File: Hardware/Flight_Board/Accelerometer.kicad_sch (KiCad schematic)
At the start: 6 parts, among them U3 ADXL375

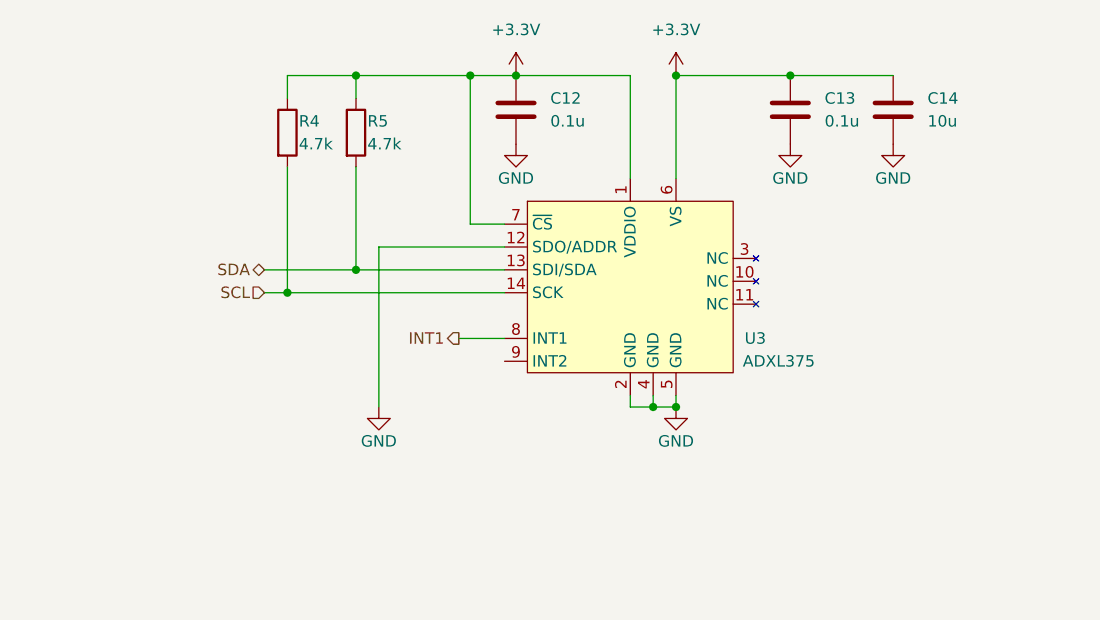
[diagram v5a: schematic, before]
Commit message: Add LEDs and test points
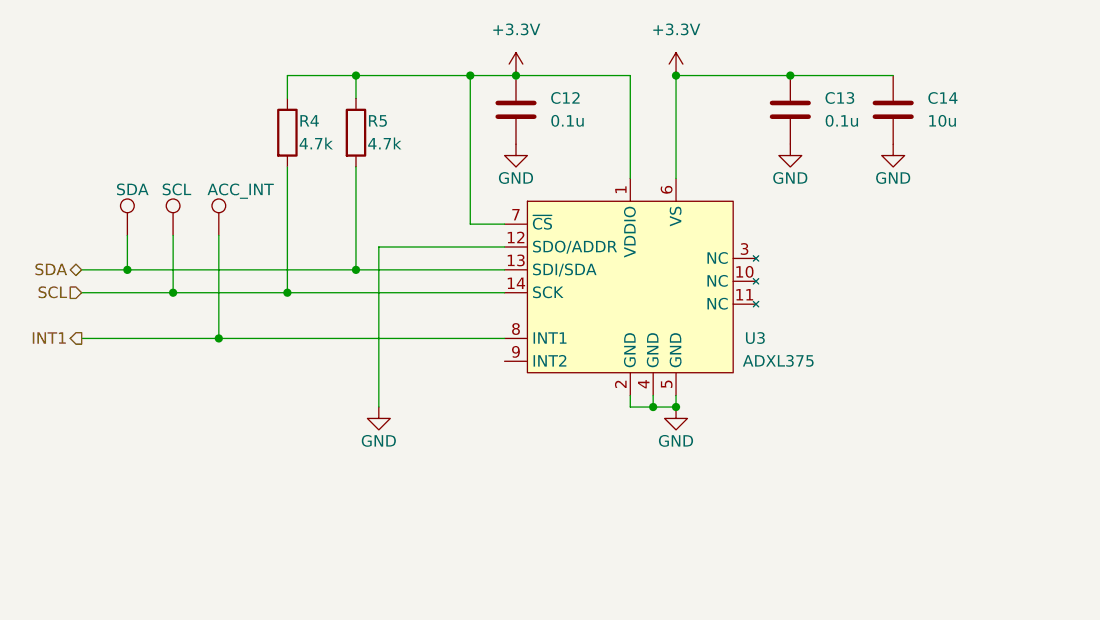
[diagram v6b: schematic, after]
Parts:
- added TP2: ACC_INT, symbol Connector:TestPoint
- added TP2: SCL, symbol Connector:TestPoint
- added TP2: SDA, symbol Connector:TestPoint
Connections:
- net INT1: now also TP2.1
- net SCL: now also TP2.1
- net SDA: now also TP2.1
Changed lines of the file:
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@@
   (junction (at 179.07 55.88) (diameter 0) (color 0 0 0 0)
   )
+  (junction (at 118.11 77.47) (diameter 0) (color 0 0 0 0)
+  )
   (junction (at 143.51 55.88) (diameter 0) (color 0 0 0 0)
   )
+  (junction (at 128.27 85.09) (diameter 0) (color 0 0 0 0)
+  )
   (junction (at 143.51 77.47) (diameter 0) (color 0 0 0 0)
   )
@@
   (junction (at 161.29 55.88) (diameter 0) (color 0 0 0 0)
   )
+  (junction (at 123.19 80.01) (diameter 0) (color 0 0 0 0)
+  )
   (junction (at 135.89 80.01) (diameter 0) (color 0 0 0 0)
   )
   (junction (at 176.53 92.71) (diameter 0) (color 0 0 0 0)
   )
+  (wire (pts (xy 128.27 85.09) (xy 160.02 85.09))
+    (stroke (width 0) (type default))
+  )
   (wire (pts (xy 160.02 72.39) (xy 156.21 72.39))
     (stroke (width 0) (type default))
   )
-  (wire (pts (xy 133.35 80.01) (xy 135.89 80.01))
+  (wire (pts (xy 113.03 80.01) (xy 123.19 80.01))
+    (stroke (width 0) (type default))
+  )
+  (wire (pts (xy 123.19 73.66) (xy 123.19 80.01))
     (stroke (width 0) (type default))
   )
@@
     (stroke (width 0) (type default))
   )
+  (wire (pts (xy 128.27 73.66) (xy 128.27 85.09))
+    (stroke (width 0) (type default))
+  )
   (wire (pts (xy 179.07 92.71) (xy 176.53 92.71))
     (stroke (width 0) (type default))
@@
     (stroke (width 0) (type default))
   )
-  (wire (pts (xy 154.94 85.09) (xy 160.02 85.09))
+  (wire (pts (xy 113.03 85.09) (xy 128.27 85.09))
     (stroke (width 0) (type default))
   )
@@
     (stroke (width 0) (type default))
   )
+  (wire (pts (xy 118.11 77.47) (xy 143.51 77.47))
+    (stroke (width 0) (type default))
+  )
+  (wire (pts (xy 118.11 73.66) (xy 118.11 77.47))
+    (stroke (width 0) (type default))
+  )
+  (wire (pts (xy 123.19 80.01) (xy 135.89 80.01))
+    (stroke (width 0) (type default))
+  )
   (wire (pts (xy 156.21 55.88) (xy 161.29 55.88))
     (stroke (width 0) (type default))
   )
-  (wire (pts (xy 133.35 77.47) (xy 143.51 77.47))
+  (wire (pts (xy 113.03 77.47) (xy 118.11 77.47))
     (stroke (width 0) (type default))
   )
@@
     (stroke (width 0) (type default))
   )
-  (hierarchical_label "SDA" (shape bidirectional) (at 133.35 77.47 180) (fields_autoplaced)
+  (hierarchical_label "SDA" (shape bidirectional) (at 113.03 77.47 180) (fields_autoplaced)
     (effects (font (size 1.27 1.27)) (justify right))
   )
-  (hierarchical_label "INT1" (shape output) (at 154.94 85.09 180) (fields_autoplaced)
+  (hierarchical_label "INT1" (shape output) (at 113.03 85.09 180) (fields_autoplaced)
     (effects (font (size 1.27 1.27)) (justify right))
   )
-  (hierarchical_label "SCL" (shape input) (at 133.35 80.01 180) (fields_autoplaced)
+  (hierarchical_label "SCL" (shape input) (at 113.03 80.01 180) (fields_autoplaced)
     (effects (font (size 1.27 1.27)) (justify right))
   )
@@
     )
   )
+  (symbol (lib_id "Connector:TestPoint") (at 128.27 73.66 0) (unit 1)
+    (in_bom yes) (on_board yes) (dnp no)
+    (property "Reference" "TP2" (at 133.35 70.358 90)
+      (effects (font (size 1.27 1.27)) hide)
+    )
+    (property "Value" "ACC_INT" (at 127 68.58 0)
+      (effects (font (size 1.27 1.27)) (justify left))
+    )
+    (property "Footprint" "" (at 133.35 73.66 0)
+      (effects (font (size 1.27 1.27)) hide)
+    )
+    (property "Datasheet" "~" (at 133.35 73.66 0)
+      (effects (font (size 1.27 1.27)) hide)
+    )
+    (pin "1")
+    (instances
+      (project "Flight_Board"
+        (path "/e8eb85d5-f1ff-4500-895d-25b9ff5f6d36/bc23ea56-d50e-4ce7-856f-e38dfbe72971"
+          (reference "TP2") (unit 1)
+        )
+        (path "/e8eb85d5-f1ff-4500-895d-25b9ff5f6d36/43c0adf1-436b-4b66-9010-44cf9a79cc96"
+          (reference "TP5") (unit 1)
+        )
+      )
+    )
+  )
   (symbol (lib_id "power:+3.3V") (at 161.29 55.88 0) (unit 1)
     (in_bom yes) (on_board yes) (dnp no) (fields_autoplaced)
@@
     )
   )
+  (symbol (lib_id "Connector:TestPoint") (at 123.19 73.66 0) (unit 1)
+    (in_bom yes) (on_board yes) (dnp no)
+    (property "Reference" "TP2" (at 128.27 70.358 90)
+      (effects (font (size 1.27 1.27)) hide)
+    )
+    (property "Value" "SCL" (at 121.92 68.58 0)
+      (effects (font (size 1.27 1.27)) (justify left))
+    )
+    (property "Footprint" "" (at 128.27 73.66 0)
+      (effects (font (size 1.27 1.27)) hide)
+    )
+    (property "Datasheet" "~" (at 128.27 73.66 0)
+      (effects (font (size 1.27 1.27)) hide)
+    )
+    (pin "1")
+    (instances
+      (project "Flight_Board"
+        (path "/e8eb85d5-f1ff-4500-895d-25b9ff5f6d36/bc23ea56-d50e-4ce7-856f-e38dfbe72971"
+          (reference "TP2") (unit 1)
+        )
+        (path "/e8eb85d5-f1ff-4500-895d-25b9ff5f6d36/43c0adf1-436b-4b66-9010-44cf9a79cc96"
+          (reference "TP4") (unit 1)
+        )
+      )
+    )
+  )
   (symbol (lib_id "power:GND") (at 161.29 63.5 0) (unit 1)
     (in_bom yes) (on_board yes) (dnp no)
@@
         )
       )
+    )
+  )
+  (symbol (lib_id "Connector:TestPoint") (at 118.11 73.66 0) (unit 1)
+    (in_bom yes) (on_board yes) (dnp no)
+    (property "Reference" "TP2" (at 123.19 70.358 90)
+      (effects (font (size 1.27 1.27)) hide)
+    )
+    (property "Value" "SDA" (at 116.84 68.58 0)
+      (effects (font (size 1.27 1.27)) (justify left))
+    )
+    (property "Footprint" "" (at 123.19 73.66 0)
+      (effects (font (size 1.27 1.27)) hide)
+    )
+    (property "Datasheet" "~" (at 123.19 73.66 0)
+      (effects (font (size 1.27 1.27)) hide)
+    )
+    (pin "1")
+    (instances
+      (project "Flight_Board"
+        (path "/e8eb85d5-f1ff-4500-895d-25b9ff5f6d36/bc23ea56-d50e-4ce7-856f-e38dfbe72971"
+          (reference "TP2") (unit 1)
+        )
+        (path "/e8eb85d5-f1ff-4500-895d-25b9ff5f6d36/43c0adf1-436b-4b66-9010-44cf9a79cc96"
+          (reference "TP3") (unit 1)
+        )
+      )

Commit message: final touches, bom, footprints
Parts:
- C12, C13, C14: footprint (none) -> Capacitor_SMD:C_0603_1608Metric_Pad1.08x0.95mm_HandSolder
- R4, R5: footprint (none) -> Resistor_SMD:R_0603_1608Metric_Pad0.98x0.95mm_HandSolder
- TP2: footprint (none) -> TestPoint:TestPoint_THTPad_2.0x2.0mm_Drill1.0mm
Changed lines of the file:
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@@
       (effects (font (size 1.27 1.27)) (justify left))
     )
-    (property "Footprint" "" (at 141.732 62.23 90)
+    (property "Footprint" "Resistor_SMD:R_0603_1608Metric_Pad0.98x0.95mm_HandSolder" (at 141.732 62.23 90)
       (effects (font (size 1.27 1.27)) hide)
     )
@@
       (effects (font (size 1.27 1.27)) (justify right))
     )
-    (property "Footprint" "" (at 160.3248 55.88 0)
+    (property "Footprint" "Capacitor_SMD:C_0603_1608Metric_Pad1.08x0.95mm_HandSolder" (at 160.3248 55.88 0)
       (effects (font (size 1.27 1.27)) hide)
     )
@@
       (effects (font (size 1.27 1.27)) (justify left))
     )
-    (property "Footprint" "" (at 204.1652 63.5 0)
+    (property "Footprint" "Capacitor_SMD:C_0603_1608Metric_Pad1.08x0.95mm_HandSolder" (at 204.1652 63.5 0)
       (effects (font (size 1.27 1.27)) hide)
     )
@@
       (effects (font (size 1.27 1.27)) (justify left))
     )
-    (property "Footprint" "" (at 133.35 73.66 0)
+    (property "Footprint" "TestPoint:TestPoint_THTPad_2.0x2.0mm_Drill1.0mm" (at 133.35 73.66 0)
       (effects (font (size 1.27 1.27)) hide)
     )
@@
       (effects (font (size 1.27 1.27)) (justify left))
     )
-    (property "Footprint" "" (at 128.27 73.66 0)
+    (property "Footprint" "TestPoint:TestPoint_THTPad_2.0x2.0mm_Drill1.0mm" (at 128.27 73.66 0)
       (effects (font (size 1.27 1.27)) hide)
     )
@@
       (effects (font (size 1.27 1.27)) (justify left))
     )
-    (property "Footprint" "" (at 192.7352 63.5 0)
+    (property "Footprint" "Capacitor_SMD:C_0603_1608Metric_Pad1.08x0.95mm_HandSolder" (at 192.7352 63.5 0)
       (effects (font (size 1.27 1.27)) hide)
     )
@@
       (effects (font (size 1.27 1.27)) (justify left))
     )
-    (property "Footprint" "" (at 134.112 62.23 90)
+    (property "Footprint" "Resistor_SMD:R_0603_1608Metric_Pad0.98x0.95mm_HandSolder" (at 134.112 62.23 90)
       (effects (font (size 1.27 1.27)) hide)
     )
@@
       (effects (font (size 1.27 1.27)) (justify left))
     )
-    (property "Footprint" "" (at 123.19 73.66 0)
-      (effects (font (size 1.27 1.27)) hide)
-    )
+    (property "Footprint" "TestPoint:TestPoint_THTPad_2.0x2.0mm_Drill1.0mm" (at 123.19 73.66 0)
+      (effects (font (size 1.27 1.27)) hide)
+    )

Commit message: initial route of 4-layer board
ouch
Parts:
- renumbered R4 to R7, R5 to R8
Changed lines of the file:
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@@
   (symbol (lib_id "Device:R") (at 143.51 62.23 0) (unit 1)
     (in_bom yes) (on_board yes) (dnp no)
-    (property "Reference" "R5" (at 144.78 60.96 0)
+    (property "Reference" "R8" (at 144.78 60.96 0)
       (effects (font (size 1.27 1.27)) (justify left))
     )
@@
       (project "Flight_Board"
         (path "/e8eb85d5-f1ff-4500-895d-25b9ff5f6d36/43c0adf1-436b-4b66-9010-44cf9a79cc96"
-          (reference "R5") (unit 1)
+          (reference "R8") (unit 1)
         )
       )
@@
   (symbol (lib_id "power:GND") (at 146.05 92.71 0) (unit 1)
     (in_bom yes) (on_board yes) (dnp no)
-    (property "Reference" "#PWR020" (at 146.05 99.06 0)
+    (property "Reference" "#PWR025" (at 146.05 99.06 0)
       (effects (font (size 1.27 1.27)) hide)
     )
@@
       (project "Flight_Board"
         (path "/e8eb85d5-f1ff-4500-895d-25b9ff5f6d36/43c0adf1-436b-4b66-9010-44cf9a79cc96"
-          (reference "#PWR020") (unit 1)
+          (reference "#PWR025") (unit 1)
         )
       )
@@
   (symbol (lib_id "power:GND") (at 203.2 63.5 0) (unit 1)
     (in_bom yes) (on_board yes) (dnp no)
-    (property "Reference" "#PWR026" (at 203.2 69.85 0)
+    (property "Reference" "#PWR031" (at 203.2 69.85 0)
       (effects (font (size 1.27 1.27)) hide)
     )
@@
       (project "Flight_Board"
         (path "/e8eb85d5-f1ff-4500-895d-25b9ff5f6d36/43c0adf1-436b-4b66-9010-44cf9a79cc96"
-          (reference "#PWR026") (unit 1)
+          (reference "#PWR031") (unit 1)
         )
       )
@@
   (symbol (lib_id "power:GND") (at 191.77 63.5 0) (unit 1)
     (in_bom yes) (on_board yes) (dnp no)
-    (property "Reference" "#PWR025" (at 191.77 69.85 0)
+    (property "Reference" "#PWR030" (at 191.77 69.85 0)
       (effects (font (size 1.27 1.27)) hide)
     )
@@
       (project "Flight_Board"
         (path "/e8eb85d5-f1ff-4500-895d-25b9ff5f6d36/43c0adf1-436b-4b66-9010-44cf9a79cc96"
-          (reference "#PWR025") (unit 1)
+          (reference "#PWR030") (unit 1)
         )
       )
@@
         )
         (path "/e8eb85d5-f1ff-4500-895d-25b9ff5f6d36/43c0adf1-436b-4b66-9010-44cf9a79cc96"
-          (reference "TP5") (unit 1)
+          (reference "TP12") (unit 1)
         )
       )
@@
   (symbol (lib_id "power:+3.3V") (at 161.29 55.88 0) (unit 1)
     (in_bom yes) (on_board yes) (dnp no) (fields_autoplaced)
-    (property "Reference" "#PWR021" (at 161.29 59.69 0)
+    (property "Reference" "#PWR026" (at 161.29 59.69 0)
       (effects (font (size 1.27 1.27)) hide)
     )
@@
       (project "Flight_Board"
         (path "/e8eb85d5-f1ff-4500-895d-25b9ff5f6d36/43c0adf1-436b-4b66-9010-44cf9a79cc96"
-          (reference "#PWR021") (unit 1)
+          (reference "#PWR026") (unit 1)
         )
       )
@@
   (symbol (lib_id "power:+3.3V") (at 179.07 55.88 0) (unit 1)
     (in_bom yes) (on_board yes) (dnp no) (fields_autoplaced)
-    (property "Reference" "#PWR023" (at 179.07 59.69 0)
+    (property "Reference" "#PWR028" (at 179.07 59.69 0)
       (effects (font (size 1.27 1.27)) hide)
     )
@@
       (project "Flight_Board"
         (path "/e8eb85d5-f1ff-4500-895d-25b9ff5f6d36/43c0adf1-436b-4b66-9010-44cf9a79cc96"
-          (reference "#PWR023") (unit 1)
+          (reference "#PWR028") (unit 1)
         )
       )
@@
         )
         (path "/e8eb85d5-f1ff-4500-895d-25b9ff5f6d36/43c0adf1-436b-4b66-9010-44cf9a79cc96"
-          (reference "TP4") (unit 1)
+          (reference "TP11") (unit 1)
         )
       )
@@
   (symbol (lib_id "power:GND") (at 161.29 63.5 0) (unit 1)
     (in_bom yes) (on_board yes) (dnp no)
-    (property "Reference" "#PWR022" (at 161.29 69.85 0)
+    (property "Reference" "#PWR027" (at 161.29 69.85 0)
       (effects (font (size 1.27 1.27)) hide)
     )
@@
       (project "Flight_Board"
         (path "/e8eb85d5-f1ff-4500-895d-25b9ff5f6d36/43c0adf1-436b-4b66-9010-44cf9a79cc96"
-          (reference "#PWR022") (unit 1)
+          (reference "#PWR027") (unit 1)
         )
       )
@@
   (symbol (lib_id "Device:R") (at 135.89 62.23 0) (unit 1)
     (in_bom yes) (on_board yes) (dnp no)
-    (property "Reference" "R4" (at 137.16 60.96 0)
+    (property "Reference" "R7" (at 137.16 60.96 0)
       (effects (font (size 1.27 1.27)) (justify left))
     )
@@
       (project "Flight_Board"
         (path "/e8eb85d5-f1ff-4500-895d-25b9ff5f6d36/43c0adf1-436b-4b66-9010-44cf9a79cc96"
-          (reference "R4") (unit 1)
+          (reference "R7") (unit 1)
         )
       )
@@
   (symbol (lib_id "power:GND") (at 179.07 92.71 0) (unit 1)
     (in_bom yes) (on_board yes) (dnp no)
-    (property "Reference" "#PWR024" (at 179.07 99.06 0)
+    (property "Reference" "#PWR029" (at 179.07 99.06 0)
       (effects (font (size 1.27 1.27)) hide)
     )
@@
       (project "Flight_Board"
         (path "/e8eb85d5-f1ff-4500-895d-25b9ff5f6d36/43c0adf1-436b-4b66-9010-44cf9a79cc96"
-          (reference "#PWR024") (unit 1)
+          (reference "#PWR029") (unit 1)
         )
       )
@@
         )
         (path "/e8eb85d5-f1ff-4500-895d-25b9ff5f6d36/43c0adf1-436b-4b66-9010-44cf9a79cc96"
-          (reference "TP3") (unit 1)
-        )
-      )
+          (reference "TP10") (unit 1)
+        )
+      )
